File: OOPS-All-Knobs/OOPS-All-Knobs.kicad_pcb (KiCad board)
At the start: 2 copper layers, 228 x 76 mm, 155 parts

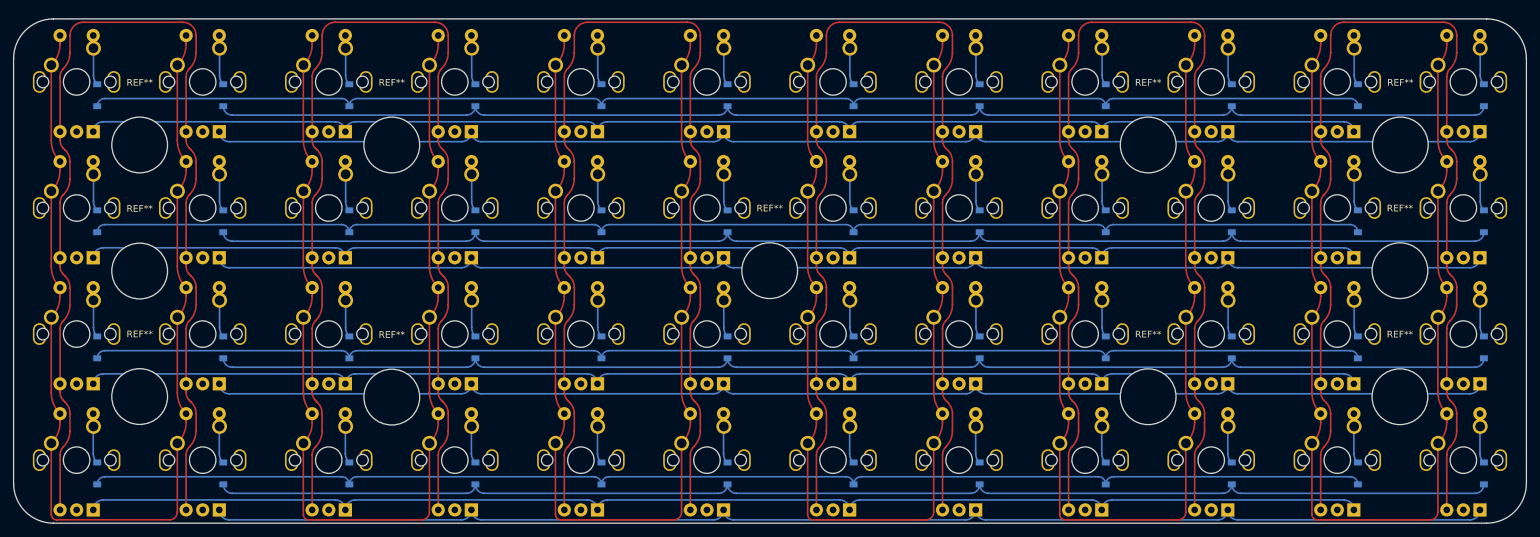
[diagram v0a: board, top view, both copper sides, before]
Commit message: Added Planck footprint
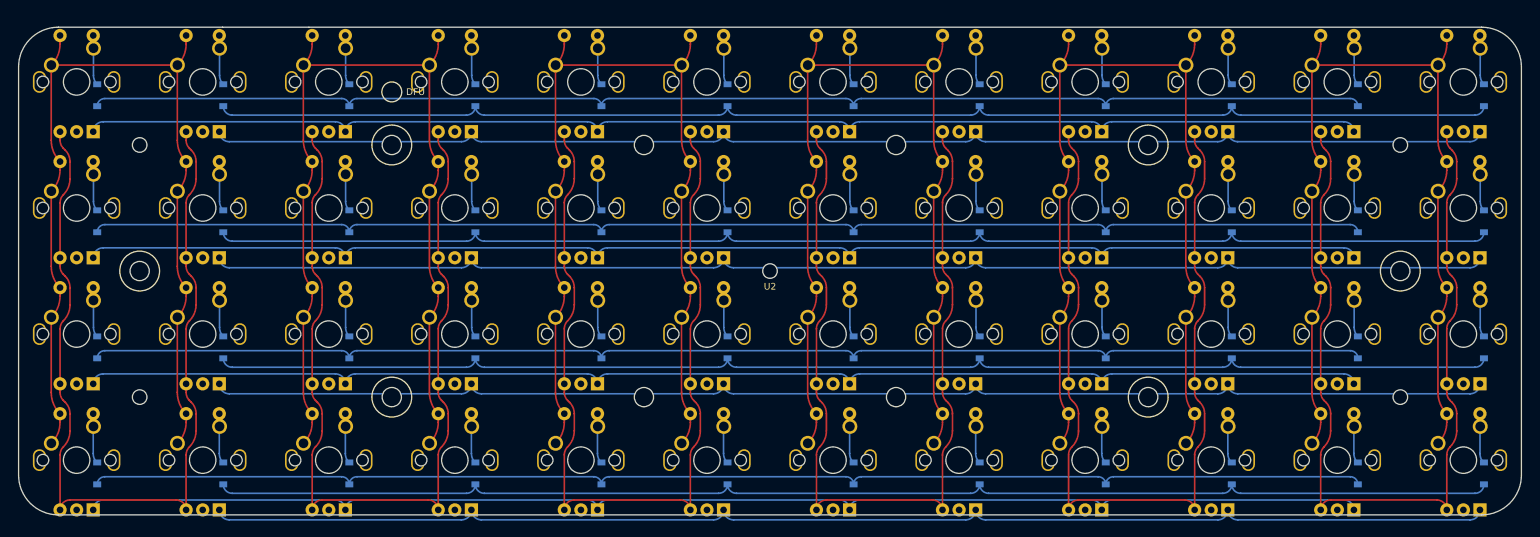
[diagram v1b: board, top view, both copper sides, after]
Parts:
- removed REF** (x11): MountingHole_8.4mm_M8, MountingHole:MountingHole_8.4mm_M8
- added U2: planck-pcb-module, Keebio-Parts:planck-pcb-module, F.Cu at (138.5, 56.5)
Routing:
- net REC4: track 169.7 -> 139.4 mm
- net REC5: track 169.7 -> 139.4 mm
- net REC1: track 169.7 -> 139.4 mm
- net REC3: track 169.7 -> 139.4 mm
- net REC0: track 169.7 -> 139.4 mm
- net REC2: track 169.7 -> 139.4 mm
- net SWC5: track 168.3 -> 146.2 mm
- net SWC4: track 168.3 -> 146.2 mm
- net SWC3: track 168.3 -> 146.2 mm
- net SWC0: track 170.9 -> 148.8 mm
- net SWC2: track 168.3 -> 146.2 mm
- net SWC1: track 168.3 -> 146.2 mm
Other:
- board size 228 x 76 mm -> 226.5 x 73.5 mm

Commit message: Placed and routed controller
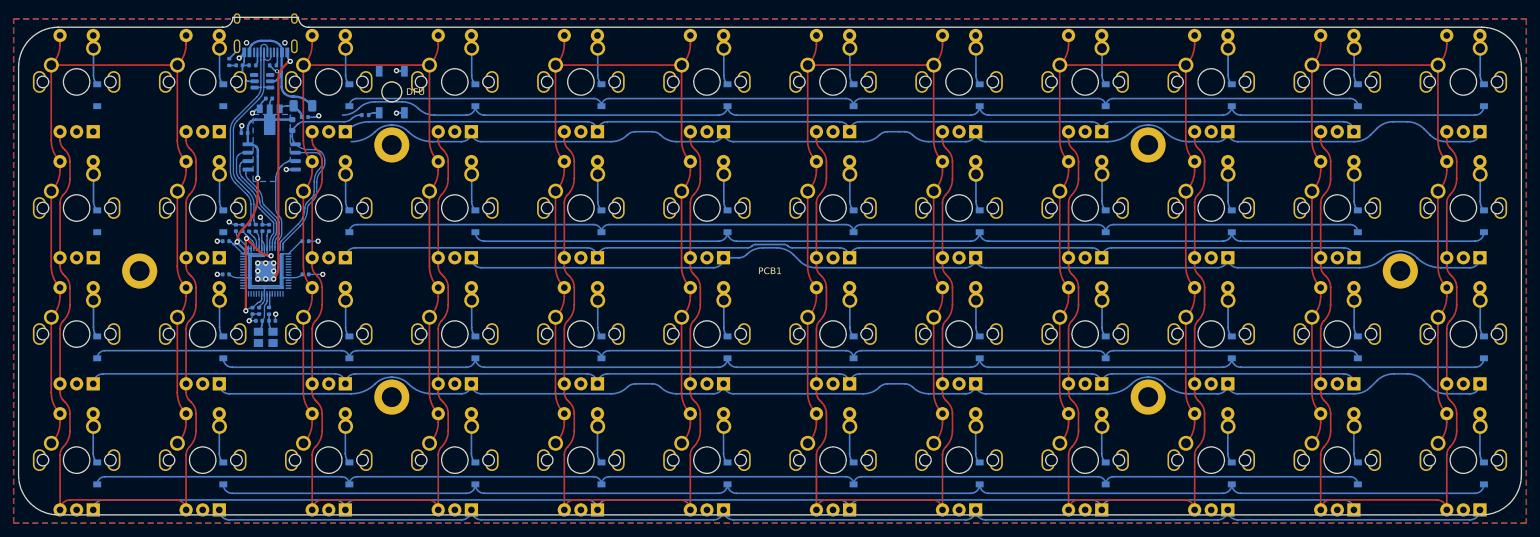
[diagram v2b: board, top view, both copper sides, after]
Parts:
- added C1: 10u, Capacitor_SMD:C_0402_1005Metric, B.Cu at (68.4, 33.3)
- added C10: 100n, Capacitor_SMD:C_0402_1005Metric, B.Cu at (61.5, 62.5)
- added C11: 100n, Capacitor_SMD:C_0402_1005Metric, B.Cu at (62.0, 50.0)
- added C12: 100n, Capacitor_SMD:C_0402_1005Metric, B.Cu at (56.5, 52.0)
- added C13: 100n, Capacitor_SMD:C_0402_1005Metric, B.Cu at (56.5, 57.0)
- added C14: 100n, Capacitor_SMD:C_0402_1005Metric, B.Cu at (68.5, 52.0)
- added C17: 1u, Capacitor_SMD:C_0402_1005Metric, B.Cu at (58.0, 50.0)
- added C18: 1u, Capacitor_SMD:C_0402_1005Metric, B.Cu at (59.0, 50.0)
- added C2: 10u, Capacitor_SMD:C_0402_1005Metric, B.Cu at (63.0, 30.5)
- added C3: 0.1u, Capacitor_SMD:C_0402_1005Metric, B.Cu at (58.5, 25.5)
- added C4: 100n, Capacitor_SMD:C_0402_1005Metric, B.Cu at (59.3, 35.7)
- added C5: 27p, Capacitor_SMD:C_0402_1005Metric, B.Cu at (61.5, 64.0)
- added C6: 27p, Capacitor_SMD:C_0402_1005Metric, B.Cu at (63.5, 64.0)
- added C7: 100n, Capacitor_SMD:C_0402_1005Metric, B.Cu at (60.5, 62.5)
- added C8: 100n, Capacitor_SMD:C_0402_1005Metric, B.Cu at (63.0, 50.0)
- added C9: 100n, Capacitor_SMD:C_0402_1005Metric, B.Cu at (68.5, 57.0)
- added F1: 500mA, Fuse:Fuse_1206_3216Metric, B.Cu at (68.1, 31.6)
- added J1: USB_C_Receptacle_USB2.0, Connector_USB:USB_C_Receptacle_HRO_TYPE-C-31-M-12, B.Cu at (62.5, 19.5)
- added R1: 5.1k, Resistor_SMD:R_0402_1005Metric, B.Cu at (60.5, 25.5)
- added R2: 5.1k, Resistor_SMD:R_0402_1005Metric, B.Cu at (63.6, 25.5)
- added R3: 1M, Resistor_SMD:R_0402_1005Metric, B.Cu at (57.0, 25.0)
- added R4: -10k, Resistor_SMD:R_0603_1608Metric, B.Cu at (66.5, 34.5)
- added R5: 1k, Resistor_SMD:R_0402_1005Metric, B.Cu at (77.5, 33.0)
- added R6: 27, Resistor_SMD:R_0402_1005Metric, B.Cu at (60.0, 50.0)
- added R7: 27, Resistor_SMD:R_0402_1005Metric, B.Cu at (61.0, 50.0)
- added R8: 1k, Resistor_SMD:R_0402_1005Metric, B.Cu at (63.0, 62.5)
- added SW1: SW_SPST, Keebio-Parts:SW_SPST_TL3342, B.Cu at (81.5, 29.5)
- added U1: NCP1117-3.3_SOT223, Package_TO_SOT_SMD:SOT-89-3, B.Cu at (63.1, 33.7)
- added U2: W25Q128JVS, Package_SO:SOIC-8_5.23x5.23mm_P1.27mm, B.Cu at (63.4, 39.3)
- added U3: RP2040TR7, SnapEDA Library:QFN40P700X700X90-57N, B.Cu at (62.5, 56.5)
- added U4: SRV05-4, marbastlib-various:SOT-23-6-routable, B.Cu at (62.0, 27.9)
- added Y1: 12MHz, Crystal:Crystal_SMD_3225-4Pin_3.2x2.5mm, B.Cu at (62.5, 66.5)
- renumbered U2 to PCB1
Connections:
- ENC1 pad C: unconnected-(ENC1-PadC) -> GND
- ENC10 pad C: unconnected-(ENC10-PadC) -> GND
- ENC11 pad C: unconnected-(ENC11-PadC) -> GND
- ENC12 pad C: unconnected-(ENC12-PadC) -> GND
- ENC13 pad C: unconnected-(ENC13-PadC) -> GND
- ENC14 pad C: unconnected-(ENC14-PadC) -> GND
- ENC15 pad C: unconnected-(ENC15-PadC) -> GND
- ENC16 pad C: unconnected-(ENC16-PadC) -> GND
- ENC17 pad C: unconnected-(ENC17-PadC) -> GND
- ENC18 pad C: unconnected-(ENC18-PadC) -> GND
- ENC19 pad C: unconnected-(ENC19-PadC) -> GND
- ENC2 pad C: unconnected-(ENC2-PadC) -> GND
- ENC20 pad C: unconnected-(ENC20-PadC) -> GND
- ENC21 pad C: unconnected-(ENC21-PadC) -> GND
- ENC22 pad C: unconnected-(ENC22-PadC) -> GND
- ENC23 pad C: unconnected-(ENC23-PadC) -> GND
- ENC24 pad C: unconnected-(ENC24-PadC) -> GND
- ENC25 pad C: unconnected-(ENC25-PadC) -> GND
- ENC26 pad C: unconnected-(ENC26-PadC) -> GND
- ENC27 pad C: unconnected-(ENC27-PadC) -> GND
- ENC28 pad C: unconnected-(ENC28-PadC) -> GND
- ENC29 pad C: unconnected-(ENC29-PadC) -> GND
- ENC3 pad C: unconnected-(ENC3-PadC) -> GND
- ENC30 pad C: unconnected-(ENC30-PadC) -> GND
- ENC31 pad C: unconnected-(ENC31-PadC) -> GND
- ENC32 pad C: unconnected-(ENC32-PadC) -> GND
- ENC33 pad C: unconnected-(ENC33-PadC) -> GND
- ENC34 pad C: unconnected-(ENC34-PadC) -> GND
- ENC35 pad C: unconnected-(ENC35-PadC) -> GND
- ENC36 pad C: unconnected-(ENC36-PadC) -> GND
- ENC37 pad C: unconnected-(ENC37-PadC) -> GND
- ENC38 pad C: unconnected-(ENC38-PadC) -> GND
- ENC39 pad C: unconnected-(ENC39-PadC) -> GND
- ENC4 pad C: unconnected-(ENC4-PadC) -> GND
- ENC40 pad C: unconnected-(ENC40-PadC) -> GND
- ENC41 pad C: unconnected-(ENC41-PadC) -> GND
- ENC42 pad C: unconnected-(ENC42-PadC) -> GND
- ENC43 pad C: unconnected-(ENC43-PadC) -> GND
- ENC44 pad C: unconnected-(ENC44-PadC) -> GND
- ENC45 pad C: unconnected-(ENC45-PadC) -> GND
- ENC46 pad C: unconnected-(ENC46-PadC) -> GND
- ENC47 pad C: unconnected-(ENC47-PadC) -> GND
- ENC48 pad C: unconnected-(ENC48-PadC) -> GND
- ENC5 pad C: unconnected-(ENC5-PadC) -> GND
- ENC6 pad C: unconnected-(ENC6-PadC) -> GND
- ENC7 pad C: unconnected-(ENC7-PadC) -> GND
- ENC8 pad C: unconnected-(ENC8-PadC) -> GND
- ENC9 pad C: unconnected-(ENC9-PadC) -> GND
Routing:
- net +3V3: track 0.00 -> 123.7 mm, vias 0 -> 2
- net GND: track 0.00 -> 79.5 mm, vias 0 -> 25
- net ENR0: track 198.0 -> 157.9 mm
- net SWR3: track 197.2 -> 157.7 mm
- net ENR2: track 198.0 -> 158.6 mm
- net SWR2: track 196.1 -> 156.9 mm
- net SWR0: track 196.1 -> 156.9 mm
- net ENR3: track 198.0 -> 160.1 mm
- net QSPI_SS: track 0.00 -> 34.4 mm
- net D+: track 0.00 -> 32.7 mm
- net D-: track 0.00 -> 32.7 mm
- net +1V1: track 0.00 -> 27.7 mm, vias 0 -> 3
- net VBUS: track 0.00 -> 20.7 mm
- net QSPI_D1: track 0.00 -> 20.0 mm
- net QSPI_D3: track 0.00 -> 17.8 mm
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- added copper zone on B.Cu, net +3V3
- added copper zone on B.Cu, net GND
- added copper zone on F.Cu, net GND
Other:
- board size 226.5 x 73.5 mm -> 226.5 x 75 mm

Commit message: Some progress on routing matrices
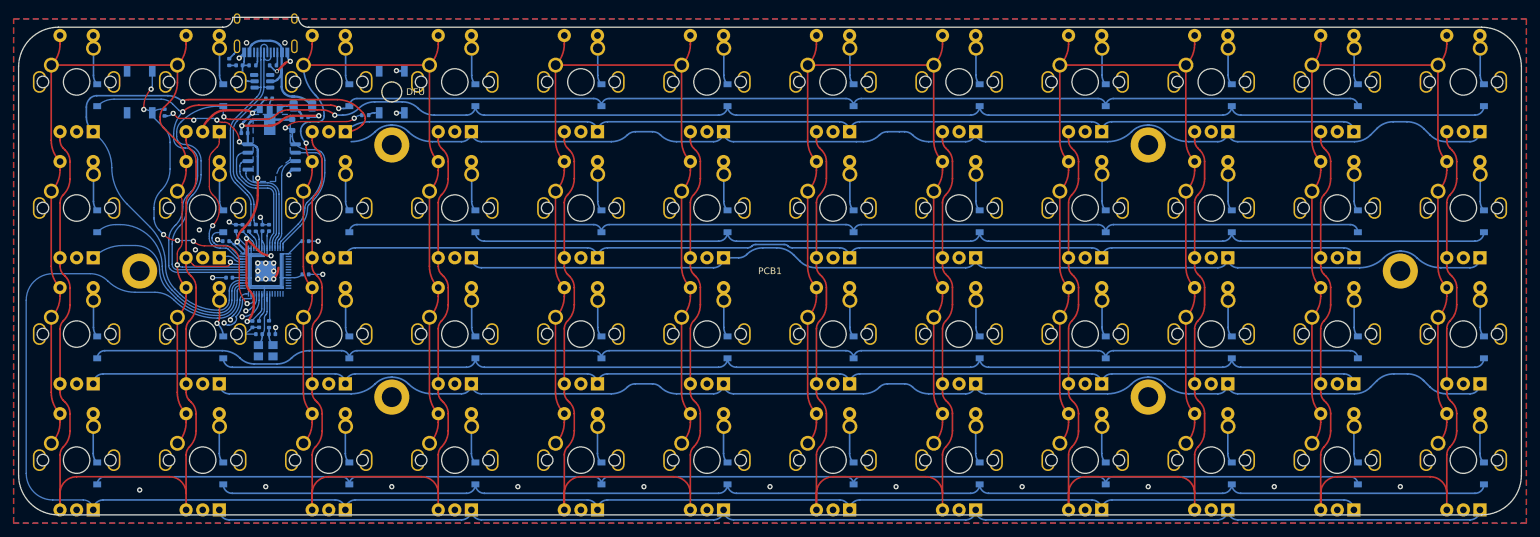
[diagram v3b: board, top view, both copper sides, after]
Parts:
- added R9: 5.1k, Resistor_SMD:R_0402_1005Metric, B.Cu at (47.3, 32.6)
- added SW2: SW_SPST, Keebio-Parts:SW_SPST_TL3342, B.Cu at (43.5, 29.5)
- moved C10 2.01 mm to (61.5, 64.5)
- moved C5 2.01 mm to (61.5, 66.0)
- moved C6 2.01 mm to (63.5, 66.0)
- moved C7 2.01 mm to (60.5, 64.5)
- moved R8 2.01 mm to (63.0, 64.5)
- moved Y1 2.01 mm to (62.5, 68.5)
- moved C13 0.71 mm to (57.0, 57.5)
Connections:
- U3 pad 26: unconnected-(U3-Pad26) -> RUN
- U3 pad 29: unconnected-(U3-Pad29) -> ENR6
- U3 pad 30: unconnected-(U3-Pad30) -> ENR2
- U3 pad 31: unconnected-(U3-Pad31) -> SWR2
- U3 pad 32: unconnected-(U3-Pad32) -> ENR0
- U3 pad 35: unconnected-(U3-Pad35) -> SWR0
- U3 pad 36: unconnected-(U3-Pad36) -> SWR1
- U3 pad 37: unconnected-(U3-Pad37) -> SWC0
- U3 pad 38: unconnected-(U3-Pad38) -> REC0
- U3 pad 39: unconnected-(U3-Pad39) -> ENR3
- U3 pad 40: unconnected-(U3-Pad40) -> ENR1
- U3 pad 41: unconnected-(U3-Pad41) -> SWR3
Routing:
- net ENR0: track 157.9 -> 252.1 mm, vias 0 -> 1
- net ENR6: track 198.0 -> 276.6 mm
- net SWR0: track 156.9 -> 234.9 mm, vias 0 -> 2
- net SWR1: track 179.5 -> 242.4 mm, vias 0 -> 2
- net RUN: track 0.00 -> 52.0 mm, vias 0 -> 6
- net SWR2: track 156.9 -> 189.0 mm
- net ENR2: track 158.6 -> 189.9 mm
- net ENR1: track 183.1 -> 207.0 mm, vias 0 -> 1
- net +3V3: track 123.7 -> 140.2 mm, vias 2 -> 6
- net REC0: track 139.4 -> 152.5 mm, vias 0 -> 1
- net SWC0: track 148.8 -> 161.1 mm, vias 0 -> 1
- net SWR3: track 157.7 -> 165.8 mm
- net unconnected-(U3-Pad27): track 0.00 -> 7.67 mm, vias 0 -> 1
- net unconnected-(U3-Pad28): track 0.00 -> 5.19 mm, vias 0 -> 1
- net unconnected-(U3-Pad24): track 0.00 -> 4.90 mm, vias 0 -> 1
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
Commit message: routed controller, just a few connections left
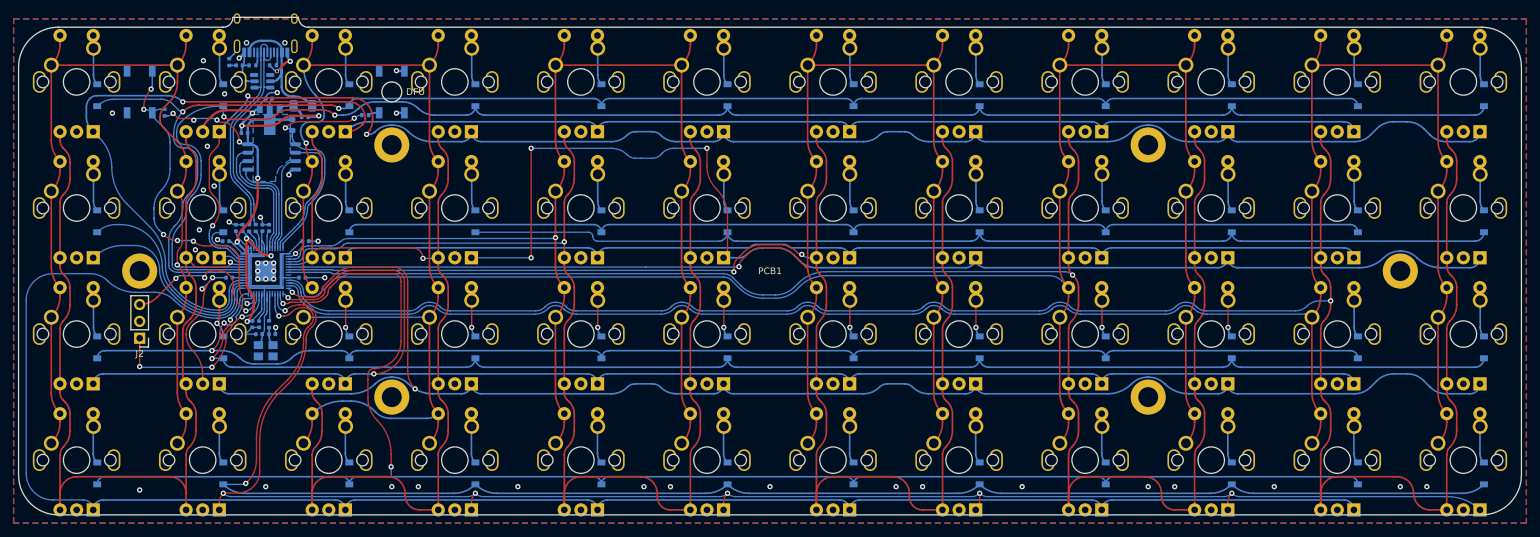
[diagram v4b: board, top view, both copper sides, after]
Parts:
- added J2: Conn_01x03_Female, Connector_PinHeader_2.54mm:PinHeader_1x03_P2.54mm_Vertical, F.Cu at (43.5, 66.6)
- moved C9 0.71 mm to (68.0, 57.5)
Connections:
- U3 pad 11: unconnected-(U3-Pad11) -> SWC4
- U3 pad 12: unconnected-(U3-Pad12) -> REC5
- U3 pad 13: unconnected-(U3-Pad13) -> SWC5
- U3 pad 14: unconnected-(U3-Pad14) -> ENR5
- U3 pad 15: unconnected-(U3-Pad15) -> ENR4
- U3 pad 16: unconnected-(U3-Pad16) -> SWR6
- U3 pad 17: unconnected-(U3-Pad17) -> ENR7
- U3 pad 18: unconnected-(U3-Pad18) -> SWR7
- U3 pad 2: unconnected-(U3-Pad2) -> SWC1
- U3 pad 24: unconnected-(U3-Pad24) -> SWCLK
- U3 pad 25: unconnected-(U3-Pad25) -> SWDIO
- U3 pad 27: unconnected-(U3-Pad27) -> SWR4
- U3 pad 28: unconnected-(U3-Pad28) -> SWR5
- U3 pad 3: unconnected-(U3-Pad3) -> SWC2
- U3 pad 4: unconnected-(U3-Pad4) -> REC2
- U3 pad 5: unconnected-(U3-Pad5) -> REC1
- U3 pad 6: unconnected-(U3-Pad6) -> SWC3
- U3 pad 7: unconnected-(U3-Pad7) -> REC3
- U3 pad 8: unconnected-(U3-Pad8) -> REC4
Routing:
- net REC5: track 142.9 -> 308.3 mm, vias 0 -> 1
- net SWC5: track 146.2 -> 307.2 mm
- net SWC4: track 146.2 -> 268.8 mm
- net REC4: track 142.9 -> 264.8 mm, vias 0 -> 1
- net REC3: track 142.9 -> 227.0 mm, vias 0 -> 2
- net SWC3: track 146.2 -> 227.4 mm, vias 0 -> 1
- net SWR6: track 196.1 -> 250.9 mm, vias 0 -> 2
- net ENR7: track 198.0 -> 246.2 mm, vias 0 -> 6
- net REC2: track 142.9 -> 187.4 mm, vias 0 -> 1
- net SWC2: track 146.2 -> 187.8 mm, vias 0 -> 1
- net ENR5: track 203.8 -> 241.7 mm, vias 0 -> 2
- net ENR4: track 198.0 -> 235.7 mm, vias 0 -> 2
- net SWR7: track 197.2 -> 234.6 mm, vias 0 -> 2
- net ENR3: track 164.0 -> 194.1 mm, vias 0 -> 3
- net SWCLK: track 0.00 -> 29.3 mm, vias 0 -> 3
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
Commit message: More ground stitching, pics and schematic
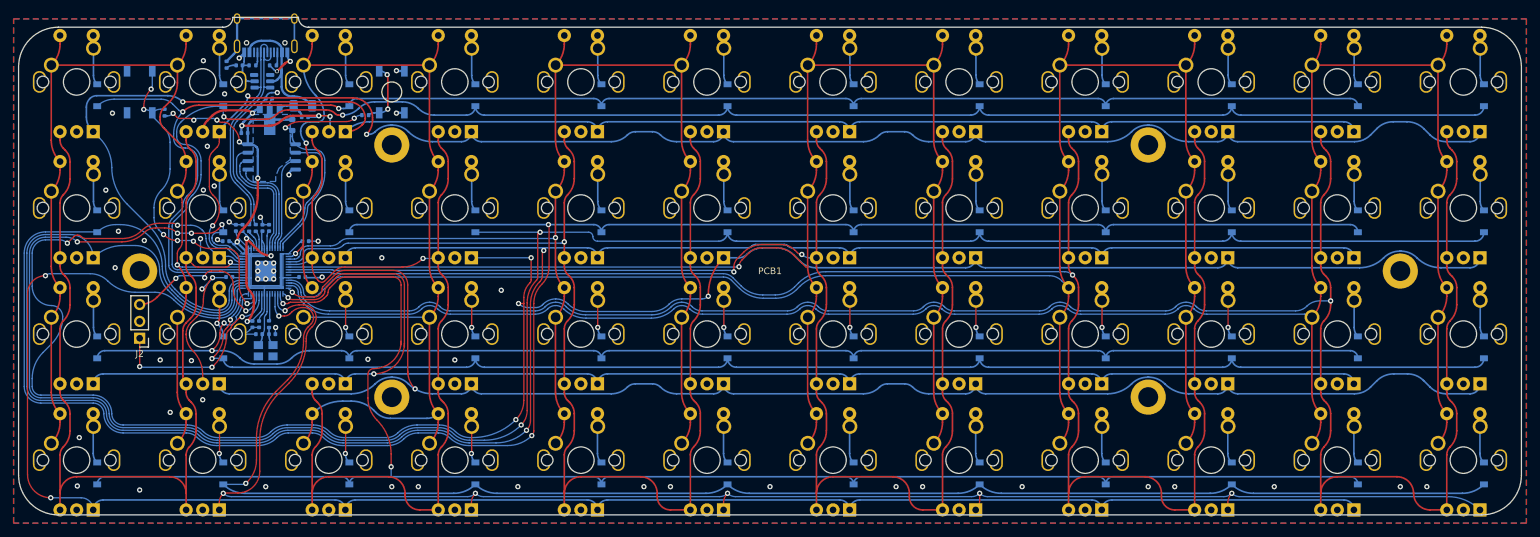
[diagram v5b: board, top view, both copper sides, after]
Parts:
- moved R3 0.57 mm to (56.6, 25.4)
- moved C13 0.10 mm to (57.0, 57.4)
- moved C9 0.10 mm to (68.0, 57.4)
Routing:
- net SWR3: track 165.8 -> 328.9 mm, vias 0 -> 6
- net SWR2: track 189.0 -> 337.2 mm, vias 0 -> 2
- net ENR2: track 189.9 -> 333.3 mm, vias 0 -> 2
- net ENR3: track 194.1 -> 331.3 mm, vias 3 -> 6
- net Net-(J1-PadS1): track 2.27 -> 19.8 mm
- net Net-(R5-Pad2): track 1.68 -> 9.70 mm, vias 0 -> 2
- net GND: track 99.0 -> 92.0 mm, vias 50 -> 64
- net SWC0: track 161.3 -> 158.3 mm
- net +3V3: track 139.6 -> 136.9 mm
- net REC2: track 187.4 -> 184.9 mm
- net REC4: track 264.8 -> 262.3 mm
- net REC3: track 227.0 -> 224.5 mm
- net REC0: track 152.9 -> 150.4 mm
- net REC5: track 308.3 -> 306.1 mm
- net VBUS: track 20.7 -> 19.6 mm
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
